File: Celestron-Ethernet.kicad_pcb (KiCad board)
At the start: 4 copper layers, 88.9 x 31.8 mm, 74 parts, among them J1 FTDI, J2 RJ45_Amphenol_RJMG1BD3B8K1ANR, J3 6P6C, SW1 SW_Push, SW2 DHCP, U1 W5500, U2 ATmega328-AU, U3 LP2985-3.3, U4 LP2985-5.0, Y1 16MHz, Y2 25MHz

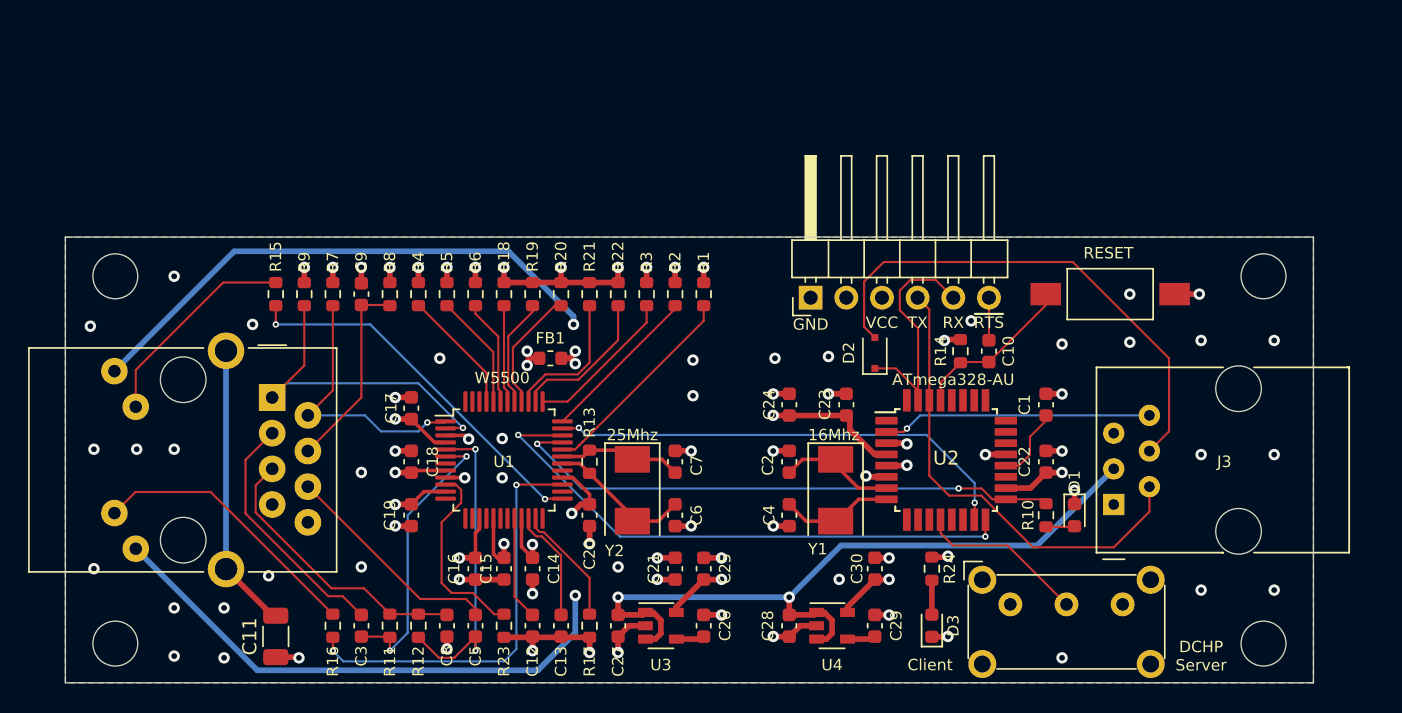
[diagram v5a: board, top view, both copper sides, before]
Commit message: schematic fixes, moved copper planes
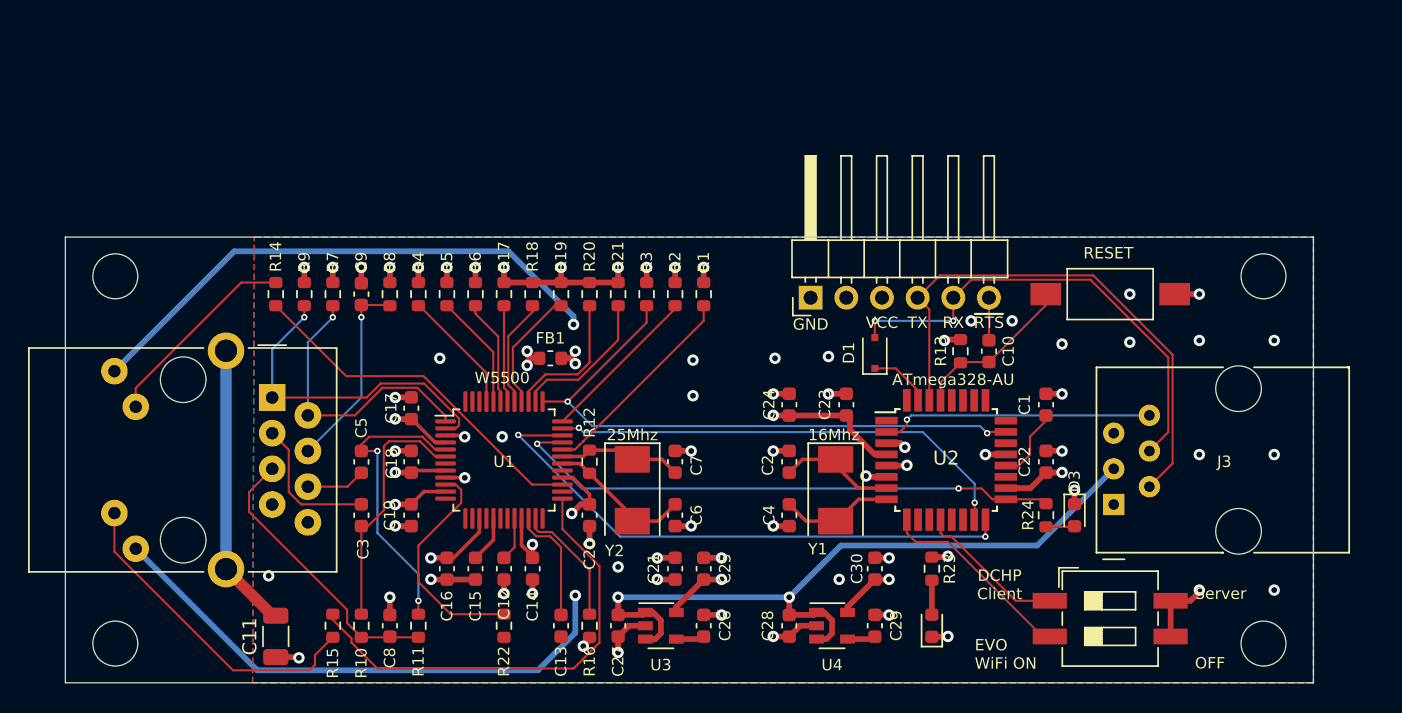
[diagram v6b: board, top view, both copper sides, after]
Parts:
- SW2: value DHCP -> SW_DIP_x02; footprint Button_Switch_THT:SW_E-Switch_EG1224_SPDT_Angled -> Button_Switch_SMD:SW_DIP_SPSTx02_Slide_6.7x6.64mm_W8.61mm_P2.54mm_LowProfile
- U2: value ATmega328-AU -> ATmega328P-AU
- moved C5 14.2 mm to (122.7, 98.6), turned to 90 degrees
- moved C3 7.87 mm to (122.7, 102.4)
- moved SW2 7.18 mm to (176.0, 109.7)
- moved C12 4.54 mm to (132.8, 106.2)
- moved C8 4.06 mm to (124.7, 110.2), turned to 270 degrees
- moved C15 2.03 mm to (130.8, 106.2)
- moved C16 2.03 mm to (128.8, 106.2)
- moved R10 2.03 mm to (122.7, 110.2), turned to 270 degrees
- turned R11 to 270 degrees
- turned R15 to 90 degrees
- renumbered D2 to D1, D3 to D2, D1 to D3, R11 to R10, R12 to R11, R13 to R12, R14 to R13, R15 to R14, R16 to R15, R17 to R16, R18 to R17, R19 to R18, R20 to R19, R21 to R20, R22 to R21, R23 to R22, R24 to R23, R10 to R24
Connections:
- net /RXN renamed /RX-
- net /RXP renamed /RX+
- C10 pad 1: /~RST -> /~RESET
- J1 pad 5: /TX -> /TXO
- R13 pad 2: /~RST -> /~RESET
- R14 pad 2: /LINKLED -> /ACTLED
- R15 pad 2: /ACTLED -> /LINKLED
- R3 pad 2: Net-(R3-Pad2) -> /~RST
- R6 pad 2: Net-(R6-Pad2) -> /~RST
- SW1 pad 2: /~RST -> /~RESET
- SW2 pad 1: Net-(SW2-Pad1) -> DCHP
- SW2 pad 2: Net-(SW2-Pad2) -> EVO
- U1 pad 37: Net-(R3-Pad2) -> /~RST
- U1 pad 43: Net-(R6-Pad2) -> /~RST
- U2 pad 12: Net-(SW2-Pad2) -> DCHP
- U2 pad 23: Net-(U2-Pad23) -> /~RST
- U2 pad 29: /~RST -> /~RESET
- U2 pad 9: Net-(U2-Pad9) -> EVO
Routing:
- net /~RST: track 11.8 -> 50.7 mm, vias 0 -> 2
- net EVO: track 0.00 -> 14.2 mm
- net /TX: track 17.4 -> 4.42 mm
- net Net-(SW2-Pad2): track 12.0 -> 0.00 mm
- net /~RESET: track 0.00 -> 11.8 mm
- net /RD-: track 16.0 -> 4.22 mm
- net Net-(R3-Pad2): track 10.9 -> 0.00 mm
- net DCHP: track 0.00 -> 10.7 mm
- net Net-(R6-Pad2): track 7.57 -> 0.00 mm
- net /RD+: track 17.8 -> 10.2 mm
- net /LINKLED: track 26.9 -> 33.1 mm, vias 2 -> 0
- net /RXI: track 33.6 -> 38.9 mm
- net Net-(C12-Pad2): track 7.40 -> 3.12 mm
- net /ACTLED: track 29.7 -> 25.7 mm, vias 2 -> 0
- net /LEDY_K: track 19.8 -> 23.2 mm
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- added copper zone on In1.Cu, net GNDPWR
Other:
- board text added: "DCHP Client"
- board text added: "EVO WiFi ON"
- board text added: "OFF"
- board text added: "Server"
- board text removed: "Client"
- board text removed: "DCHP Server"

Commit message: Added aux port pullups
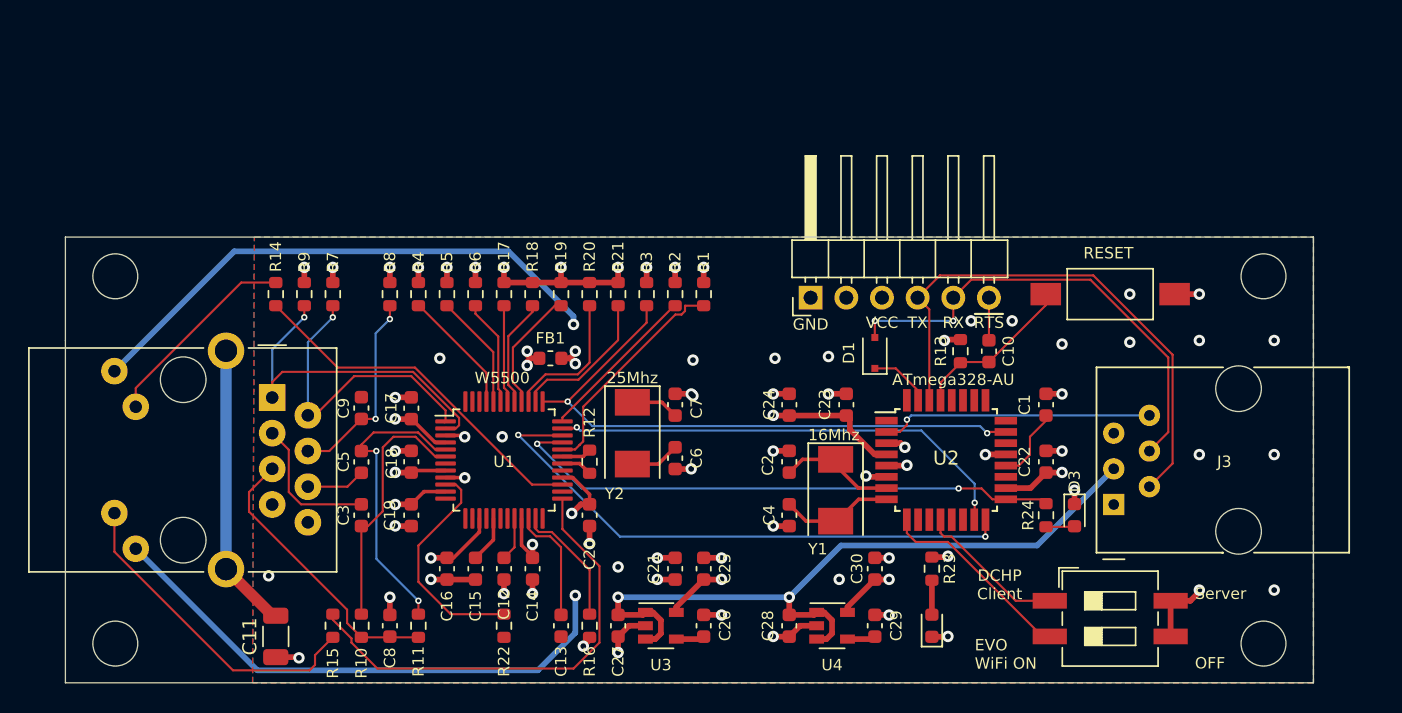
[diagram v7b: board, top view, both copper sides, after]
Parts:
- moved C9 8.11 mm to (122.7, 94.7)
- moved C7 4.06 mm to (145.0, 94.5)
- moved Y2 4.06 mm to (142.0, 96.5)
- moved C6 4.06 mm to (145.0, 98.3)
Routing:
- net Net-(C6-Pad2): track 10.4 -> 6.13 mm
- net Net-(C7-Pad2): track 8.88 -> 6.49 mm
- net /TD+: track 23.8 -> 25.2 mm
- net GND: track 64.0 -> 62.9 mm, vias 57 -> 56
- net Net-(R1-Pad2): track 14.9 -> 16.0 mm
- net /TD-: track 20.5 -> 21.4 mm
- net /TCT: track 14.0 -> 14.3 mm, vias 1 -> 2

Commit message: 3v3 version
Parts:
- removed the C16 at (128.8, 106.2)
- removed the C17 at (126.2, 94.7)
- removed C26, C29: 100nF, Capacitor_SMD:C_0603_1608Metric
- removed C28: 1uF, Capacitor_SMD:C_0603_1608Metric
- removed C30: 2.2uF, Capacitor_SMD:C_0603_1608Metric
- removed the D3 at (173.5, 102.4)
- removed the R17 at (132.8, 86.6)
- removed R18, R19, R20, R21: 10K, Resistor_SMD:R_0603_1608Metric
- removed R24: 330R, Resistor_SMD:R_0603_1608Metric
- removed the R4 at (126.7, 86.6)
- removed the R5 at (128.8, 86.6)
- removed the R6 at (130.8, 86.6)
- added D2: Grn, LED_SMD:LED_0603_1608Metric, F.Cu at (165.4, 110.2)
- added R14: 50K, Resistor_SMD:R_0603_1608Metric, F.Cu at (173.5, 94.5)
- added R15: 50K, Resistor_SMD:R_0603_1608Metric, F.Cu at (173.5, 98.6)
- C17: renamed from C19; value 100nF -> 10uF
- C24: renamed from C25; value 2.2uF -> 1uF
- D3: renamed from D2; value Blu -> Red
- FB1: value 60 ohm/100MHz -> 120 ohm/100MHz
- R16: value 10K -> 330R
- R17: renamed from R23; value 1K -> 330R
- U3: value LP2985-3.3 -> 74AHC1G125
- U4: value LP2985-5.0 -> NCV33375ST-3.3; footprint Package_TO_SOT_SMD:SOT-23-5 -> Package_TO_SOT_SMD:SOT-223
- Y1: value 16MHz -> 8MHz
- moved U3 29.0 mm to (172.1, 103.1)
- moved R16 26.7 mm to (165.4, 106.2), turned to 90 degrees
- moved C15 17.7 mm to (139.1, 90.6), turned to 90 degrees
- moved D3 16.1 mm to (147.2, 110.2)
- moved R17 16.1 mm to (147.2, 106.2)
- moved C14 15.8 mm to (133.1, 90.4), turned to 90 degrees
- moved C23 10.8 mm to (151.0, 106.2), turned to 90 degrees
- moved C24 5.66 mm to (151.0, 110.2)
- moved C22 2.03 mm to (155.2, 94.5)
- moved U4 0.99 mm to (157.0, 109.6)
- renumbered C18 to C16, C20 to C18, C21 to C19, C22 to C20, C23 to C21, C24 to C22, C27 to C23, R13 to R10, R14 to R11, R15 to R12, R22 to R13, R7 to R4, R8 to R5, R9 to R6, R10 to R7, R11 to R8, R12 to R9
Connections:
- C15 pad 1: +3.3VA -> VCC
- C18 pad 1: +3V3 -> VCC
- C19 pad 1: +3V3 -> VCC
- C20 pad 1: +5V -> VCC
- C21 pad 1: +5V -> VCC
- C22 pad 1: +5V -> VCC
- C24 pad 1: +3V3 -> VCC
- FB1 pad 2: +3V3 -> VCC
- J1 pad 3: +5V -> VCC
- J2 pad L1: +3V3 -> VCC
- J2 pad L4: +3V3 -> VCC
- R1 pad 1: +3V3 -> VCC
- R10 pad 1: +5V -> VCC
- R16 pad 1: Net-(R16-Pad1) -> Net-(D2-Pad2)
- R16 pad 2: GND -> VCC
- R17 pad 1: +5V -> VCC
- R2 pad 1: +3V3 -> VCC
- R3 pad 1: +3V3 -> VCC
- U1 pad 23: Net-(R16-Pad1) -> GND
- U1 pad 28: +3V3 -> VCC
- U1 pad 38: Net-(R21-Pad1) -> GND
- U1 pad 39: Net-(R20-Pad1) -> GND
- U1 pad 40: Net-(R19-Pad1) -> GND
- U1 pad 41: Net-(R18-Pad1) -> GND
- U1 pad 42: Net-(R17-Pad1) -> GND
- U1 pad 43: /~RST -> VCC
- U1 pad 44: Net-(R5-Pad2) -> VCC
- U1 pad 45: Net-(R4-Pad2) -> VCC
- U2 pad 18: +5V -> VCC
- U2 pad 4: +5V -> VCC
- U2 pad 6: +5V -> VCC
- U3 pad 1: +12V -> GND
- U3 pad 2: GND -> /SCK
- U3 pad 3: +12V -> GND
- U3 pad 5: +3V3 -> VCC
- U4 pad 2: GND -> +12V
- U4 pad 3: +12V -> VCC
- U4 pad 4: Net-(C29-Pad1) -> GND
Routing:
- net +3V3: track 96.2 -> 0.00 mm, vias 13 -> 0
- net VCC: track 0.00 -> 34.8 mm, vias 0 -> 7
- net GND: track 62.9 -> 32.3 mm, vias 56 -> 17
- net +5V: track 22.1 -> 0.00 mm, vias 6 -> 0
- net +12V: track 52.7 -> 34.1 mm, vias 2 -> 1
- net EVO: track 14.2 -> 0.52 mm
- net DCHP: track 10.7 -> 0.00 mm
- net Net-(R21-Pad1): track 10.6 -> 0.00 mm
- net Net-(R20-Pad1): track 9.98 -> 0.00 mm
- net Net-(R16-Pad1): track 8.95 -> 0.00 mm
- net Net-(R4-Pad2): track 8.87 -> 0.00 mm
- net Net-(R19-Pad1): track 8.76 -> 0.00 mm
- net Net-(R5-Pad2): track 8.20 -> 0.00 mm
- net Net-(R18-Pad1): track 7.73 -> 0.00 mm
- net /~RST: track 50.7 -> 43.1 mm
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- added copper zone on In2.Cu, net VCC
- removed copper zone on In2.Cu, net +3V3
- removed copper zone on In2.Cu, net +5V
